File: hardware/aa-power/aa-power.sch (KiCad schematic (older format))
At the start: 30 parts, among them CN1 12V_IN, CN2 GND_IN, CN3 12V_OUT, CN4 GND_OUT, Q1 TN1610H

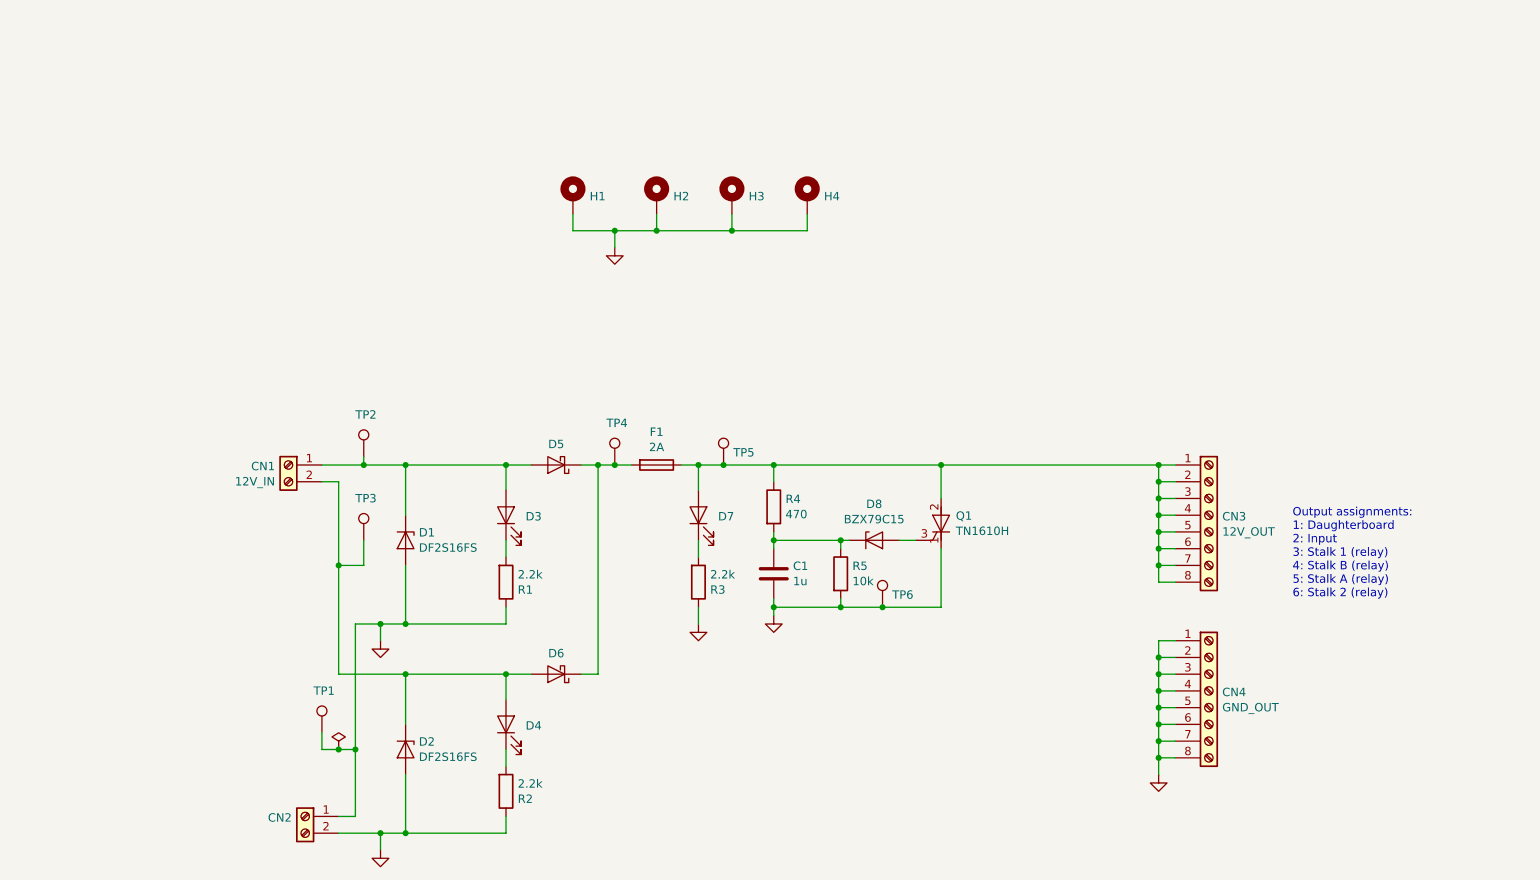
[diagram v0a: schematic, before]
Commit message: Design, lay out power protection/distribution board
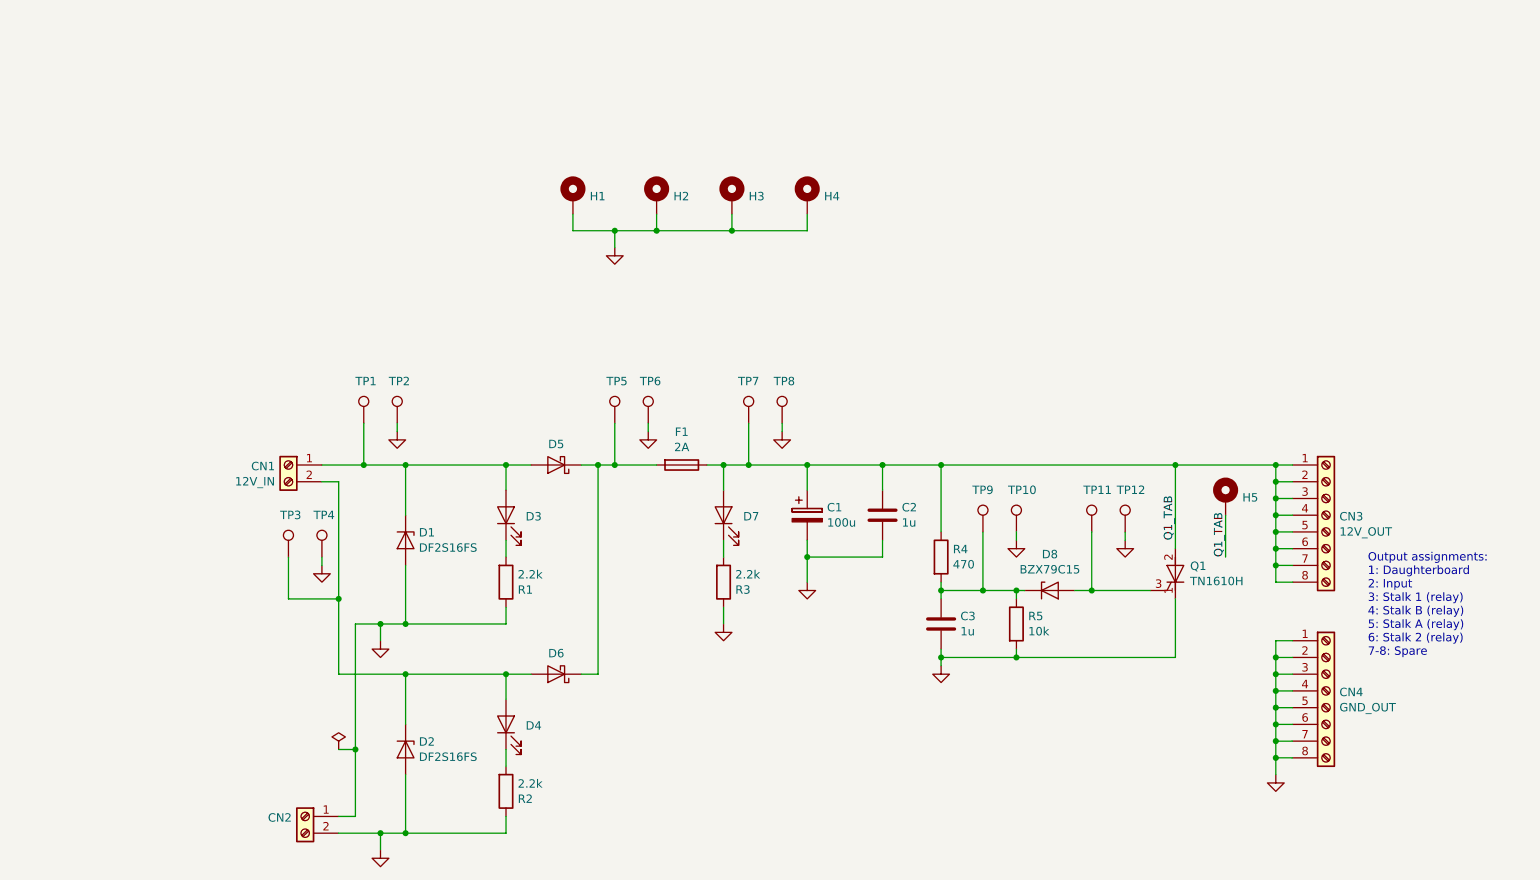
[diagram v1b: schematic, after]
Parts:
- added C1: 100u, Capacitor_THT:CP_Radial_D10.0mm_P2.50mm_P5.00mm, symbol Device:CP
- added C2: 1u, Capacitor_SMD:C_0805_2012Metric, symbol Device:C
- added H5: MountingHole_Pad, MountingHole:MountingHole_4.3mm_M4_Pad_Via, symbol Mechanical:MountingHole_Pad
- added TP10, TP12, TP4, TP6, TP8: GND, TestPoint:TestPoint_THTPad_D2.0mm_Drill1.0mm, symbol Connector:TestPoint
- added TP9: TestPoint, TestPoint:TestPoint_THTPad_D2.0mm_Drill1.0mm, symbol Connector:TestPoint
- C3: renamed from C1; footprint Capacitor_SMD:C_0603_1608Metric -> Capacitor_SMD:C_0805_2012Metric
- CN3, CN4: footprint (none) -> aa-shared:TerminalBlock_OST_OSTYK44108030
- D1, D2: footprint aa-power:D_SOD-923 -> aa-shared:D_SOD-923
- D5, D6: footprint aa-power:D_SOD-128 -> aa-shared:D_SOD-128
- F1: footprint aa-power:Fuseholder_Clip_5x20_Bel_FC-211-22 -> aa-shared:Fuseholder_Clip_5x20_Bel_FC-211-22
- Q1: footprint Package_TO_SOT_THT:TO-220-3_Vertical -> Package_TO_SOT_THT:TO-220-3_Horizontal_TabDown
- TP5: value TestPoint -> GND
- renumbered TP2 to TP1, TP4 to TP11, TP1 to TP2, TP6 to TP7
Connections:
- net GND: now also C1.2, C2.2, TP10.1, TP12.1, TP4.1, TP6.1, TP8.1; no longer TP7.1
- net Q1_TAB: now reaches CN3.1 (Pin_1), CN3.2 (Pin_2), CN3.3 (Pin_3), CN3.4 (Pin_4), CN3.5 (Pin_5), CN3.6 (Pin_6), CN3.7 (Pin_7), CN3.8 (Pin_8), D7.2 (A), F1.1, Q1.2 (A), R4.1
- net Q1_TAB: now also TP7.1, C1.1, C2.1, H5.1; no longer TP5.1
- net at D5.1 (K), D6.1 (K), F1.2: now also TP5.1; no longer TP11.1
- net at C3.1, D8.1 (K), R4.2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: now also TP9.1
- net at D8.2 (A), Q1.3 (G): now also TP11.1
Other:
- note added: "Output assignments:\n1: Daughterboard\n2: Input\n3: Stalk 1 (relay)\n4: Stalk B (relay)\n5: Stalk A (relay)\n6: Stalk 2 (relay)\n7-8: Spare"
- note removed: "Output assignments:\n1: Daughterboard\n2: Input\n3: Stalk 1 (relay)\n4: Stalk B (relay)\n5: Stalk A (relay)\n6: Stalk 2 (relay)"
- moved on the sheet: C3, CN3, CN4, D7, D8, F1, Q1, R3, R4, R5, TP1, TP11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

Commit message: Substantial rework of system, new layouts done for daughterboard, power, stalk receiver
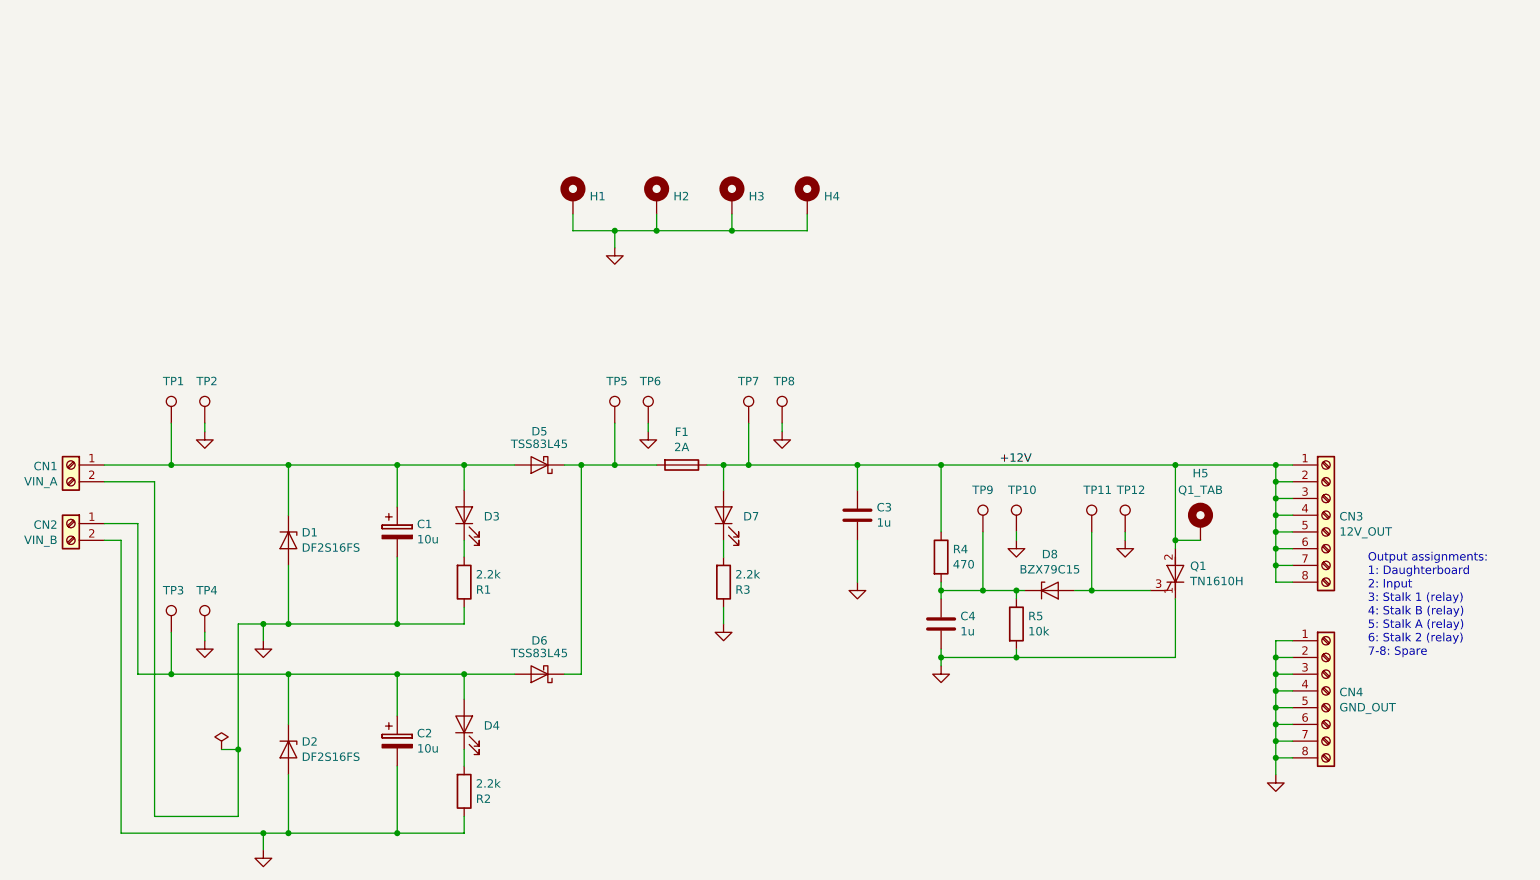
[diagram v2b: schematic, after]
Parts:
- added C2: 10u, Capacitor_THT:CP_Radial_D5.0mm_P2.50mm, symbol Device:CP
- C1: value 100u -> 10u; footprint Capacitor_THT:CP_Radial_D10.0mm_P2.50mm_P5.00mm -> Capacitor_THT:CP_Radial_D5.0mm_P2.50mm
- CN1: value 12V_IN -> VIN_A
- CN2: value GND_IN -> VIN_B
- D5, D6: value D_Schottky -> TSS83L45
- H1, H2, H3, H4: footprint MountingHole:MountingHole_4.3mm_M4_Pad_Via -> MountingHole:MountingHole_2.7mm_M2.5_Pad_Via
- H5: value MountingHole_Pad -> Q1_TAB
- renumbered C2 to C3, C3 to C4
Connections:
- net GND: now also CN1.2 (Pin_2), C2.2; no longer CN2.1 (Pin_1)
- net at CN1.1 (Pin_1), D1.1 (K), D3.2 (A)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: now also C1.1
- net at D2.1 (K), D4.2 (A), D6.2 (A)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: now also CN2.1 (Pin_1), C2.1; no longer CN1.2 (Pin_2)
- net Q1_TAB renamed +12V
- net +12V: no longer C1.1
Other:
- moved on the sheet: C3, CN1, CN2, D1, D2, D3, D4, D5, D6, H5, R1, R2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

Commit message: Final designs and actual sent gerbers for first for-real run
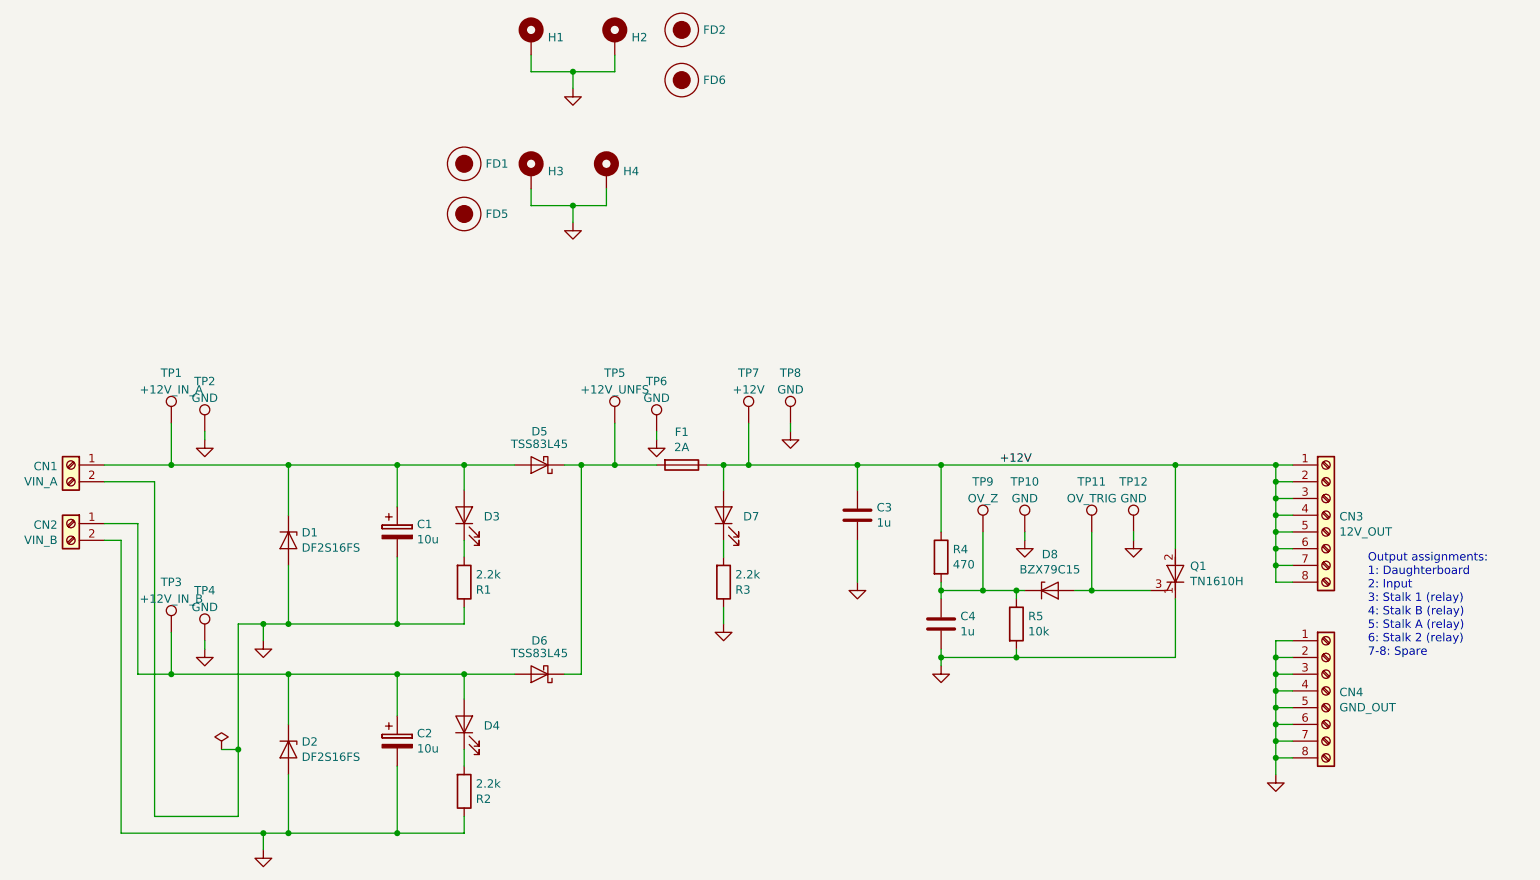
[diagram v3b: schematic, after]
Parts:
- removed H5: Q1_TAB, MountingHole:MountingHole_4.3mm_M4_Pad_Via, symbol Mechanical:MountingHole_Pad
- added FD1, FD2: Fiducial, Fiducial:Fiducial_1mm_Dia_2.54mm_Outer_CopperTop, symbol aa-shared:Fiducial
- added FD5, FD6: Fiducial, aa-shared:StencilAlignment_1.27mm, symbol aa-shared:Fiducial
- D8: footprint Diode_THT:D_DO-35_SOD27_P7.62mm_Horizontal -> Diode_THT:D_DO-35_SOD27_P2.54mm_Vertical_KathodeUp
- TP1: value 12V_IN_A -> +12V_IN_A; footprint TestPoint:TestPoint_THTPad_D2.0mm_Drill1.0mm -> aa-shared:TestPoint_Loop_D1.80mm_Drill1.0mm_Beaded
- TP10, TP12, TP2, TP4, TP6, TP8: footprint TestPoint:TestPoint_THTPad_D2.0mm_Drill1.0mm -> aa-shared:TestPoint_Loop_D1.80mm_Drill1.0mm_Beaded
- TP11: value 12V_IN -> OV_TRIG; footprint TestPoint:TestPoint_THTPad_D2.0mm_Drill1.0mm -> aa-shared:TestPoint_Loop_D1.80mm_Drill1.0mm_Beaded
- TP3: value 12V_IN_B -> +12V_IN_B; footprint TestPoint:TestPoint_THTPad_D2.0mm_Drill1.0mm -> aa-shared:TestPoint_Loop_D1.80mm_Drill1.0mm_Beaded
- TP5: value GND -> +12V_UNFS; footprint TestPoint:TestPoint_THTPad_D2.0mm_Drill1.0mm -> aa-shared:TestPoint_Loop_D1.80mm_Drill1.0mm_Beaded
- TP7: value TestPoint -> +12V; footprint TestPoint:TestPoint_THTPad_D2.0mm_Drill1.0mm -> aa-shared:TestPoint_Loop_D1.80mm_Drill1.0mm_Beaded
- TP9: value TestPoint -> OV_Z; footprint TestPoint:TestPoint_THTPad_D2.0mm_Drill1.0mm -> aa-shared:TestPoint_Loop_D1.80mm_Drill1.0mm_Beaded
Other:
- moved on the sheet: H1, H2, H3, H4, TP10, TP12, TP2, TP4, TP6, TP8
